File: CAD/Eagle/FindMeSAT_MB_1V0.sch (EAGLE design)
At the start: 127 parts, among them J291 MCX-J-P-X-RA-SM1, J685 SMA_CON, J701 MOLEX_105017-0001, J801 MICROSIM-8P_SDCARD-8P_MOLEX-1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, J901 JST_S3B-XH-A, Q101 ABS07, Q651 ABM3B-16MHZ-10-R50-1-U, U1001 CFPT-141, U101 ATXMEGA256A3BU-AU, U1011 OPA354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

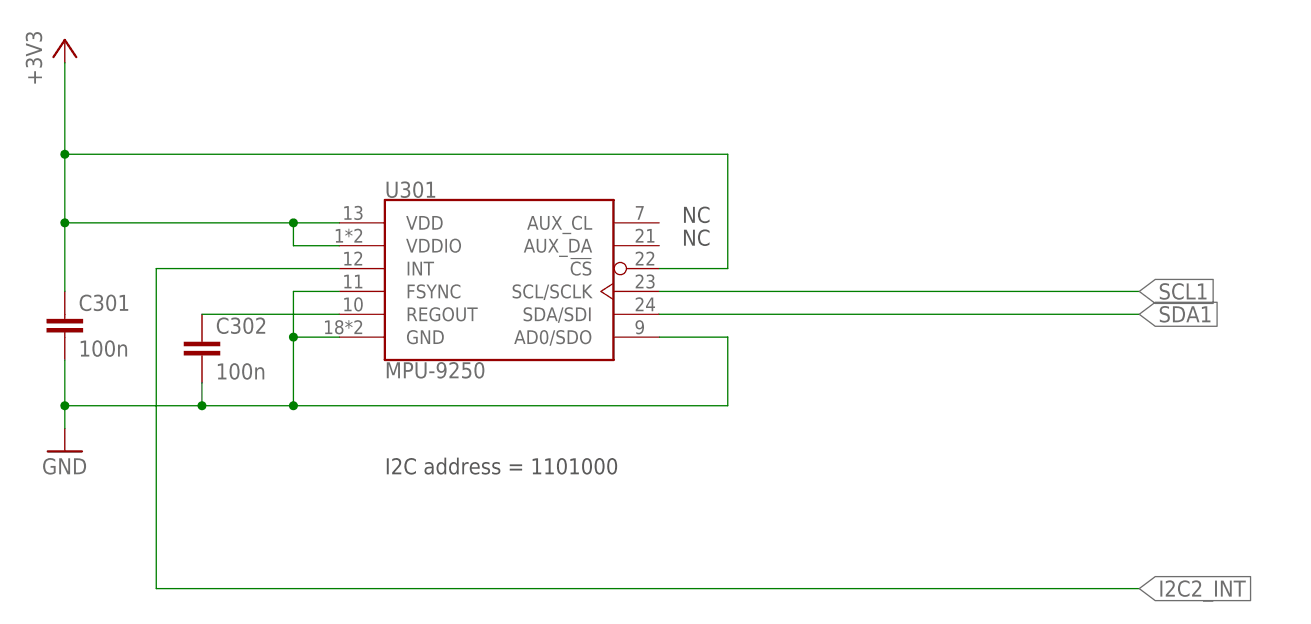
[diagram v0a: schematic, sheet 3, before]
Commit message: Eagle - some more trimming and library corrections done
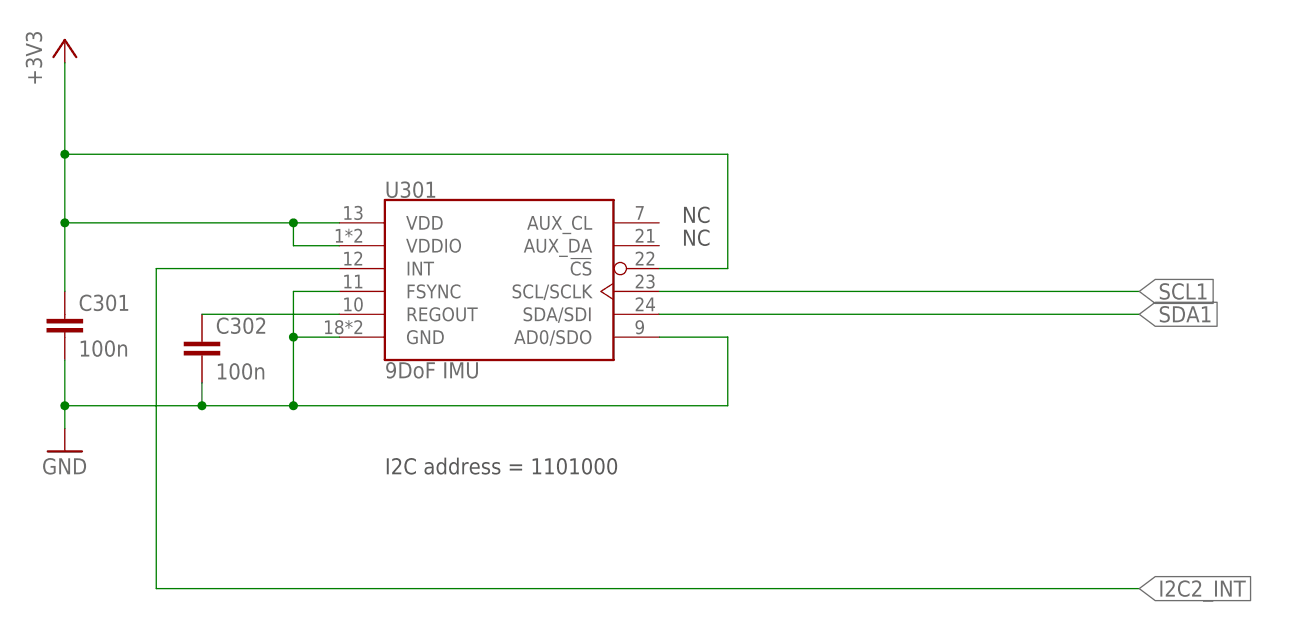
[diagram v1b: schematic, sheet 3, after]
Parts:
- U301: value MPU-9250 -> 9DoF IMU
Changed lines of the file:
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@@
 <part name="GND121" library="df4iah_supply" deviceset="GND" device=""/>
 <part name="+5V1" library="df4iah_supply" deviceset="+5V" device=""/>
-<part name="U301" library="df4iah_sensors" deviceset="MPU-9250" device="" value="MPU-9250"/>
+<part name="U301" library="df4iah_sensors" deviceset="MPU-9250" device="" value="9DoF IMU"/>
 <part name="GND311" library="df4iah_supply" deviceset="GND" device=""/>
 <part name="+3V3_311" library="df4iah_supply" deviceset="+3V3" device=""/>

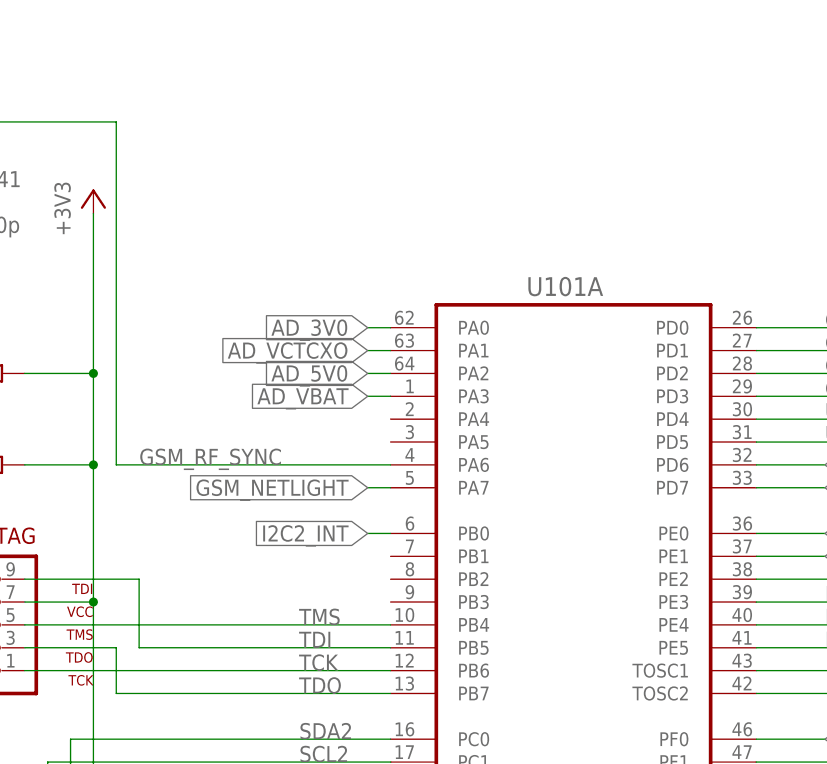
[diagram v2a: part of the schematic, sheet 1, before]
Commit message: Eagle - I/O header added
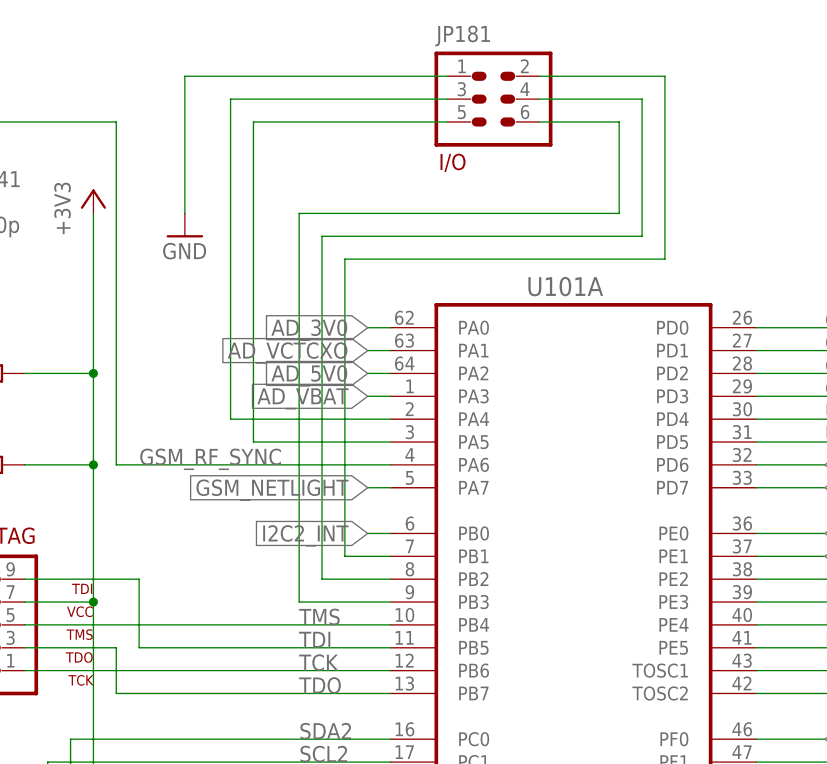
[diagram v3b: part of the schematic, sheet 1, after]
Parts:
- added JP181: HEADER-2X3, df4iah_connector:HEADER-2X3
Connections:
- new net IO_AD1: JP181.3, U101A.PA4
- new net IO_AD2: JP181.5, U101A.PA5
- new net IO_D1: JP181.2, U101A.PB1
- new net IO_D2: JP181.4, U101A.PB2
- new net IO_D3: JP181.6, U101A.PB3
- net GND: now also JP181.1
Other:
- note added: "I/O"
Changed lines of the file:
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@@
 <part name="J685" library="df4iah_connector" deviceset="SMA_SMT_AMPHENOL-901-143" device="" value="SMA_CON"/>
 <part name="GND689" library="df4iah_supply" deviceset="GND" device=""/>
+<part name="JP181" library="df4iah_connector" deviceset="HEADER-2X3" device="" value=""/>
+<part name="GND181" library="df4iah_supply" deviceset="GND" device=""/>
 </parts>
 <sheets>
@@
 <text x="5.08" y="109.22" size="1.778" layer="97">2x DAC B Audio</text>
 <text x="37.084" y="70.612" size="1.778" layer="94" ratio="10">DISPLAY</text>
+<text x="94.234" y="157.226" size="1.778" layer="94" ratio="10">I/O</text>
 </plain>
 <instances>
@@
 <instance part="GND121" gate="1" x="50.8" y="66.04"/>
 <instance part="+5V1" gate="G$1" x="25.4" y="86.36"/>
+<instance part="JP181" gate="G$1" x="100.33" y="165.1"/>
+<instance part="GND181" gate="1" x="66.04" y="149.86"/>
 </instances>
 <busses>
@@
 <wire x1="35.56" y1="81.28" x2="38.1" y2="81.28" width="0.1524" layer="91"/>
 <junction x="50.8" y="68.58"/>
+</segment>
+<segment>
+<pinref part="GND181" gate="1" pin="GND"/>
+<wire x1="66.04" y1="152.4" x2="66.04" y2="167.64" width="0.1524" layer="91"/>
+<pinref part="JP181" gate="G$1" pin="1"/>
+<wire x1="66.04" y1="167.64" x2="95.25" y2="167.64" width="0.1524" layer="91"/>
 </segment>
 </net>
@@
 </segment>
 </net>
+<net name="IO_AD1" class="0">
+<segment>
+<pinref part="U101" gate="A" pin="PA4"/>
+<wire x1="88.9" y1="129.54" x2="71.12" y2="129.54" width="0.1524" layer="91"/>
+<wire x1="71.12" y1="129.54" x2="71.12" y2="165.1" width="0.1524" layer="91"/>
+<pinref part="JP181" gate="G$1" pin="3"/>
+<wire x1="71.12" y1="165.1" x2="95.25" y2="165.1" width="0.1524" layer="91"/>
+</segment>
+</net>
+<net name="IO_AD2" class="0">
+<segment>
+<pinref part="U101" gate="A" pin="PA5"/>
+<wire x1="88.9" y1="127" x2="73.66" y2="127" width="0.1524" layer="91"/>
+<wire x1="73.66" y1="127" x2="73.66" y2="162.56" width="0.1524" layer="91"/>
+<pinref part="JP181" gate="G$1" pin="5"/>
+<wire x1="73.66" y1="162.56" x2="95.25" y2="162.56" width="0.1524" layer="91"/>
+</segment>
+</net>
+<net name="IO_D1" class="0">
+<segment>
+<pinref part="U101" gate="A" pin="PB1"/>
+<wire x1="88.9" y1="114.3" x2="83.82" y2="114.3" width="0.1524" layer="91"/>
+<wire x1="83.82" y1="114.3" x2="83.82" y2="147.32" width="0.1524" layer="91"/>
+<wire x1="83.82" y1="147.32" x2="119.38" y2="147.32" width="0.1524" layer="91"/>
+<wire x1="119.38" y1="147.32" x2="119.38" y2="167.64" width="0.1524" layer="91"/>
+<wire x1="119.38" y1="167.64" x2="105.41" y2="167.64" width="0.1524" layer="91"/>
+<pinref part="JP181" gate="G$1" pin="2"/>
+</segment>
+</net>
+<net name="IO_D2" class="0">
+<segment>
+<pinref part="U101" gate="A" pin="PB2"/>
+<wire x1="88.9" y1="111.76" x2="81.28" y2="111.76" width="0.1524" layer="91"/>
+<wire x1="81.28" y1="111.76" x2="81.28" y2="149.86" width="0.1524" layer="91"/>
+<wire x1="81.28" y1="149.86" x2="116.84" y2="149.86" width="0.1524" layer="91"/>
+<wire x1="116.84" y1="149.86" x2="116.84" y2="165.1" width="0.1524" layer="91"/>
+<wire x1="116.84" y1="165.1" x2="105.41" y2="165.1" width="0.1524" layer="91"/>
+<pinref part="JP181" gate="G$1" pin="4"/>
+</segment>
+</net>
+<net name="IO_D3" class="0">
+<segment>
+<pinref part="U101" gate="A" pin="PB3"/>
+<wire x1="88.9" y1="109.22" x2="78.74" y2="109.22" width="0.1524" layer="91"/>
+<wire x1="78.74" y1="109.22" x2="78.74" y2="152.4" width="0.1524" layer="91"/>
+<wire x1="78.74" y1="152.4" x2="114.3" y2="152.4" width="0.1524" layer="91"/>
+<wire x1="114.3" y1="152.4" x2="114.3" y2="162.56" width="0.1524" layer="91"/>
+<wire x1="114.3" y1="162.56" x2="105.41" y2="162.56" width="0.1524" layer="91"/>
+<pinref part="JP181" gate="G$1" pin="6"/>
+</segment>
+</net>

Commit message: Eagle - library entries corrected
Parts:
- C1001, C1002, C101, C1012, C1091, C1092, C1093, C1094, C1095, C1096, C1112, C1121, C301, C302, C401, C501, C601, C611, C612, C711: value 100n -> 100nF
- C1011, C141, C201, C251: value 100p -> 100pF
- C1111, C1113, C712: value 47u -> 47uF
- C681: value 68p -> 68pF
- C686: value 18p -> 18pF
- C701: value 1n -> 1nF
- C901: value 100u -> 100uF
- Q101: value ABS07 -> ABS07-32.768KHZ; device df4iah_crystal:ABS07 -> df4iah_crystal:ABS07-32.768KHZ
- R1001, R1011, R1113: value 100k -> 100kR
- R1002, R112: value 10k -> 10kR
- R1012: value 470k -> 470kR
- R1013: value 10 -> 10R
- R1021, R131, R132, R141, R142, R151, R152, R162, R163, R171, R172, R173, R221, R222, R223, R224, R231, R232, R233, R234, R241, R251: value 27 -> 27R
- R111: value 150 -> 150R
- R1111, R1131, R1141: value 4.02k -> 4.02kR
- R1112, R1132: value 6.04k -> 6.04kR
- R1114: value 15k -> 15kR
- R1115: value 68k -> 68kR
- R1142: value 2.0k -> 2.0kR
- R161: value 4.7k -> 4.7kR
- R211, R212: value 3.3k -> 3.3kR
- R701: value 330k -> 330kR
- R721: value 1k5 -> 1.5kR
- R722, R723, R725: value 68 -> 68R
- R724: value 1M -> 1MR
- RPOLY291: value 150mA -> 0A150
- RPOLY711: value 1A -> 1A0
- U1001: value CFPT-141 -> CFPT-141-20MHZ; device df4iah_osc:CFPT-141 -> df4iah_osc:CFPT-141-20MHZ
- U301: value 9DoF IMU -> MPU-9250
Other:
- note removed: "32.768 kHz"
- moved on the sheet: Q101, U1001

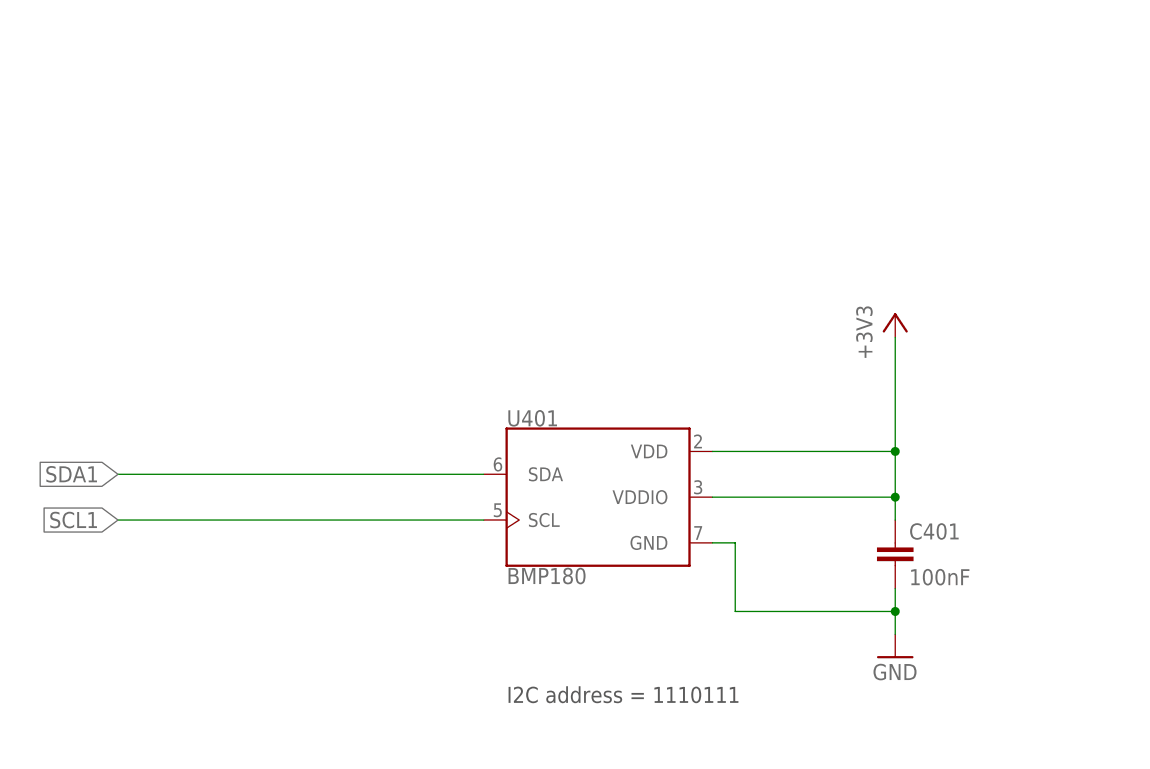
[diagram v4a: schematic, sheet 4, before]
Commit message: Eagle - new baro device placed
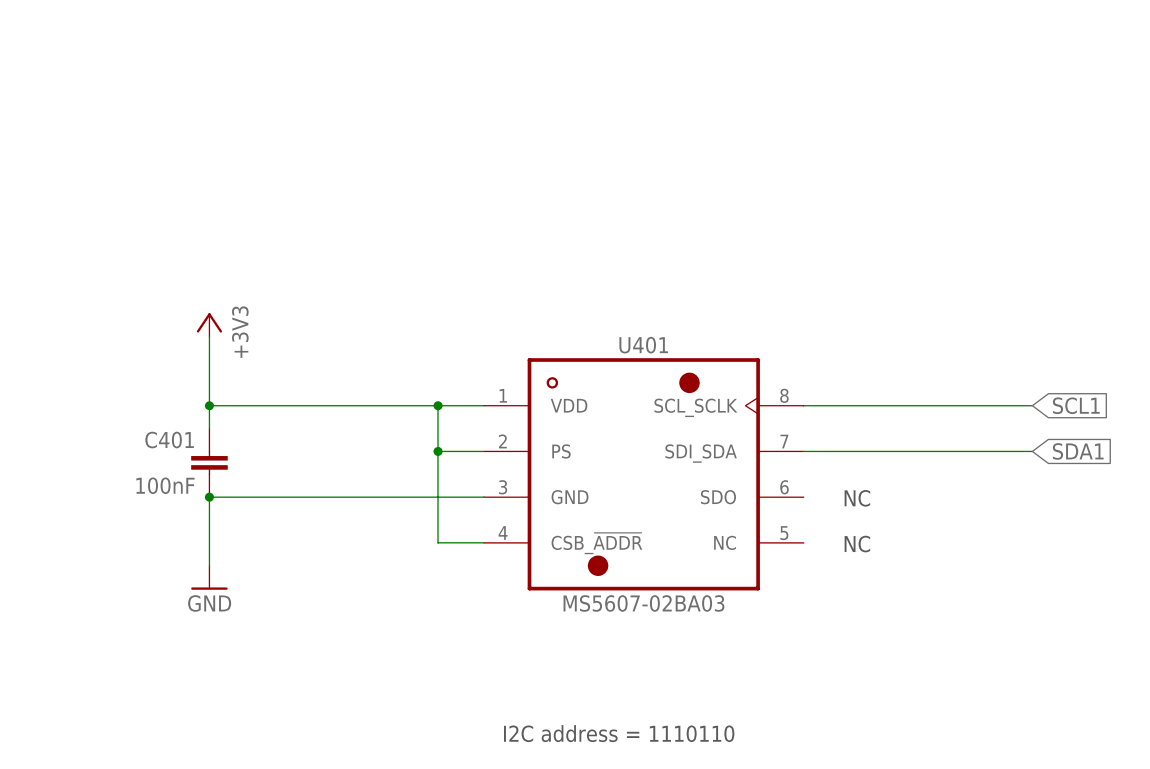
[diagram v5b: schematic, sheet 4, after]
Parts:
- U401: value BMP180 -> MS5607-02BA03; device df4iah_sensors:BMP180 -> df4iah_sensors:MS5607-02BA03
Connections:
- net +3V3: now also U401.CSB_!ADDR, U401.PS; no longer U401.VDDIO
- net SCL1: now also U401.SCL_SCLK; no longer U401.SCL
- net SDA1: now also U401.SDI_SDA; no longer U401.SDA
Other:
- note added: "I2C address = 1110110"
- note removed: "I2C address = 1110111"
- moved on the sheet: C401
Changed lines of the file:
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@@
 <part name="C301" library="rcl" deviceset="C-EU" device="C0603" value="100nF"/>
 <part name="C302" library="rcl" deviceset="C-EU" device="C0603" value="100nF"/>
-<part name="U401" library="df4iah_sensors" deviceset="BMP180" device=""/>
 <part name="GND401" library="df4iah_supply" deviceset="GND" device=""/>
 <part name="+3V3_401" library="df4iah_supply" deviceset="+3V3" device=""/>
@@
 <part name="JP181" library="df4iah_connector" deviceset="HEADER-2X3" device="" value=""/>
 <part name="GND181" library="df4iah_supply" deviceset="GND" device=""/>
+<part name="U401" library="df4iah_sensors" deviceset="MS5607-02BA" device="" technology="03"/>
 </parts>
 <sheets>
@@
 <description>Baro_Temp</description>
 <plain>
-<text x="116.84" y="68.58" size="1.778" layer="97">I2C address = 1110111</text>
+<text x="116.332" y="64.262" size="1.778" layer="97">I2C address = 1110110</text>
+<text x="154.178" y="85.344" size="1.778" layer="97">NC</text>
+<text x="154.178" y="90.424" size="1.778" layer="97">NC</text>
 </plain>
 <instances>
 <instance part="FRAME4" gate="G$1" x="0" y="0"/>
-<instance part="U401" gate="G$1" x="127" y="91.44"/>
-<instance part="GND401" gate="1" x="160.02" y="73.66"/>
-<instance part="+3V3_401" gate="G$1" x="160.02" y="111.76"/>
-<instance part="C401" gate="G$1" x="160.02" y="86.36"/>
+<instance part="GND401" gate="1" x="83.82" y="81.28" rot="MR0"/>
+<instance part="+3V3_401" gate="G$1" x="83.82" y="111.76" rot="MR0"/>
+<instance part="C401" gate="G$1" x="83.82" y="96.52" rot="MR0"/>
+<instance part="U401" gate="G$1" x="132.08" y="93.98"/>
 </instances>
 <busses>
@@
 <pinref part="GND401" gate="1" pin="GND"/>
 <pinref part="C401" gate="G$1" pin="2"/>
-<wire x1="160.02" y1="76.2" x2="160.02" y2="78.74" width="0.1524" layer="91"/>
-<wire x1="160.02" y1="78.74" x2="160.02" y2="81.28" width="0.1524" layer="91"/>
-<wire x1="160.02" y1="78.74" x2="142.24" y2="78.74" width="0.1524" layer="91"/>
-<wire x1="142.24" y1="78.74" x2="142.24" y2="86.36" width="0.1524" layer="91"/>
+<wire x1="83.82" y1="83.82" x2="83.82" y2="91.44" width="0.1524" layer="91"/>
+<wire x1="83.82" y1="91.44" x2="114.3" y2="91.44" width="0.1524" layer="91"/>
+<junction x="83.82" y="91.44"/>
 <pinref part="U401" gate="G$1" pin="GND"/>
-<wire x1="142.24" y1="86.36" x2="139.7" y2="86.36" width="0.1524" layer="91"/>
-<junction x="160.02" y="78.74"/>
 </segment>
 </net>
@@
 <pinref part="+3V3_401" gate="G$1" pin="+3V3"/>
 <pinref part="C401" gate="G$1" pin="1"/>
-<wire x1="160.02" y1="109.22" x2="160.02" y2="96.52" width="0.1524" layer="91"/>
-<pinref part="U401" gate="G$1" pin="VDDIO"/>
-<wire x1="160.02" y1="96.52" x2="160.02" y2="91.44" width="0.1524" layer="91"/>
-<wire x1="160.02" y1="91.44" x2="160.02" y2="88.9" width="0.1524" layer="91"/>
-<wire x1="160.02" y1="91.44" x2="139.7" y2="91.44" width="0.1524" layer="91"/>
+<wire x1="83.82" y1="109.22" x2="83.82" y2="101.6" width="0.1524" layer="91"/>
+<wire x1="83.82" y1="101.6" x2="83.82" y2="99.06" width="0.1524" layer="91"/>
+<wire x1="83.82" y1="101.6" x2="109.22" y2="101.6" width="0.1524" layer="91"/>
+<junction x="83.82" y="101.6"/>
 <pinref part="U401" gate="G$1" pin="VDD"/>
-<wire x1="160.02" y1="96.52" x2="139.7" y2="96.52" width="0.1524" layer="91"/>
-<junction x="160.02" y="91.44"/>
-<junction x="160.02" y="96.52"/>
+<wire x1="109.22" y1="101.6" x2="114.3" y2="101.6" width="0.1524" layer="91"/>
+<wire x1="109.22" y1="101.6" x2="109.22" y2="96.52" width="0.1524" layer="91"/>
+<pinref part="U401" gate="G$1" pin="PS"/>
+<wire x1="109.22" y1="96.52" x2="114.3" y2="96.52" width="0.1524" layer="91"/>
+<junction x="109.22" y="101.6"/>
+<wire x1="109.22" y1="96.52" x2="109.22" y2="86.36" width="0.1524" layer="91"/>
+<pinref part="U401" gate="G$1" pin="CSB_!ADDR"/>
+<wire x1="109.22" y1="86.36" x2="114.3" y2="86.36" width="0.1524" layer="91"/>
+<junction x="109.22" y="96.52"/>
 </segment>
 </net>
 <net name="SDA1" class="0">
 <segment>
-<pinref part="U401" gate="G$1" pin="SDA"/>
-<wire x1="114.3" y1="93.98" x2="73.66" y2="93.98" width="0.1524" layer="91"/>
-<label x="73.66" y="93.98" size="1.778" layer="95" rot="R180" xref="yes"/>
+<wire x1="149.86" y1="96.52" x2="175.26" y2="96.52" width="0.1524" layer="91"/>
+<label x="175.26" y="96.52" size="1.778" layer="95" xref="yes"/>
+<pinref part="U401" gate="G$1" pin="SDI_SDA"/>
 </segment>
 </net>
 <net name="SCL1" class="0">
 <segment>
-<pinref part="U401" gate="G$1" pin="SCL"/>
-<wire x1="114.3" y1="88.9" x2="73.66" y2="88.9" width="0.1524" layer="91"/>
-<label x="73.66" y="88.9" size="1.778" layer="95" rot="R180" xref="yes"/>
-</segment>
-</net>
+<wire x1="149.86" y1="101.6" x2="175.26" y2="101.6" width="0.1524" layer="91"/>
+<label x="175.26" y="101.6" size="1.778" layer="95" xref="yes"/>
+<pinref part="U401" gate="G$1" pin="SCL_SCLK"/>
+</segment>
+</net>
